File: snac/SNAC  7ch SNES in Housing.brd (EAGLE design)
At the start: 79.8 x 64.1 mm, 11 parts, among them U1 PMIC-LDO-XC6206P332MR-G(SOT23), X2 JST-XH-09-PIN-LONG-PAD

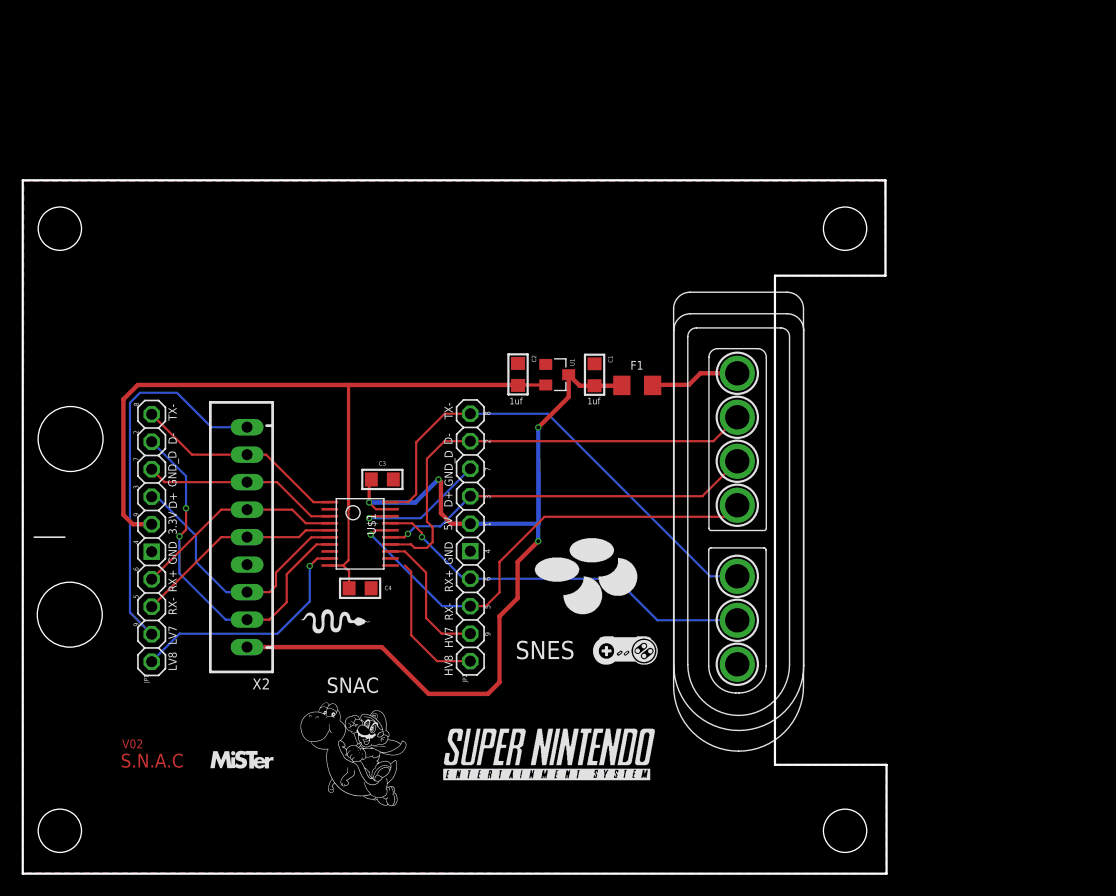
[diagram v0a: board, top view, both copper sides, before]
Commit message: Add Compact SNES version, and WIP SNES Multitap
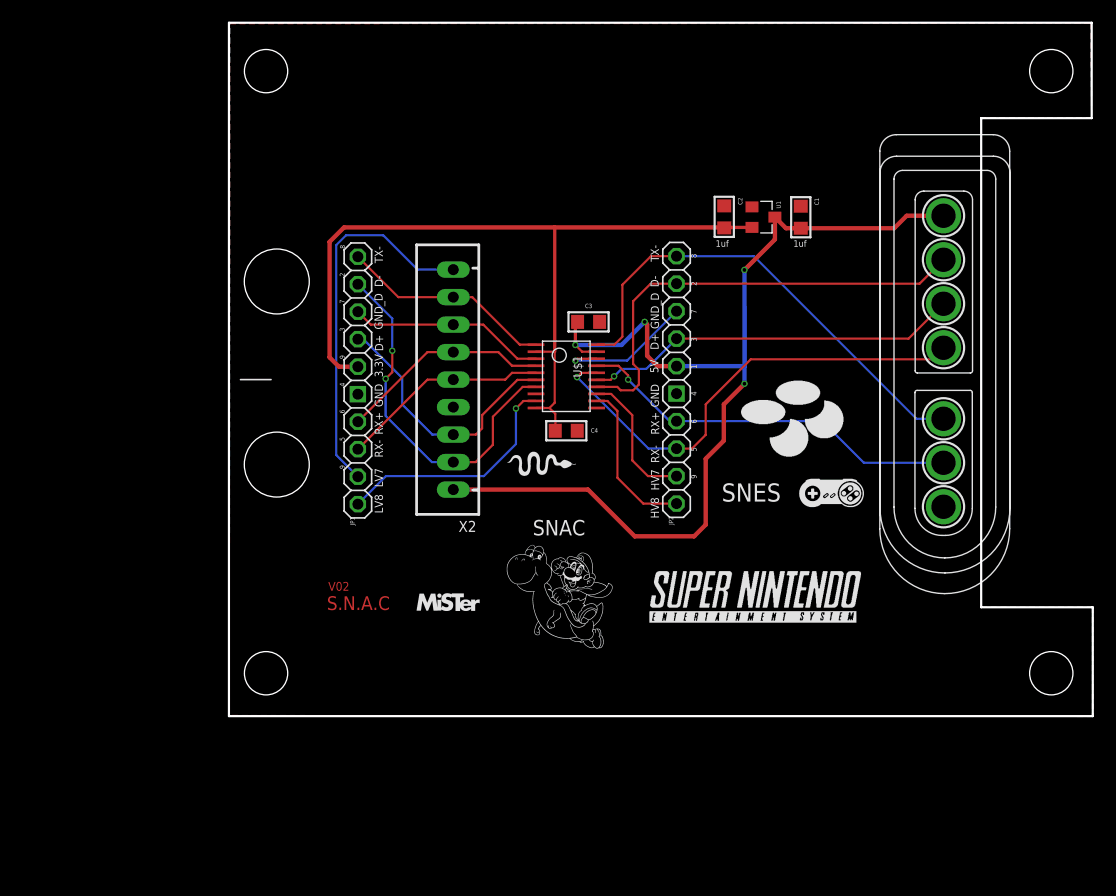
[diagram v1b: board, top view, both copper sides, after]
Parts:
- removed F1: 100mA, adafruit:R1206
- moved U$3 24.0 mm to (62.4, 46.8)
- moved JP1 24.0 mm to (12.4, 31.5)
- moved U$1 24.0 mm to (31.6, 31.9)
- moved U1 24.0 mm to (49.8, 46.6)
- moved C1 24.0 mm to (53.3, 46.6)
- moved C3 24.0 mm to (33.7, 37.0)
- moved C4 24.0 mm to (31.6, 26.9)
- moved JP2 24.0 mm to (41.8, 31.6)
- moved X2 24.0 mm to (21.2, 31.6)
- moved C2 24.0 mm to (46.2, 46.7)
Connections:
- removed net N$5: F1.2, U$3.5V
- net HV: now also U$3.5V; no longer F1.1
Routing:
- net HV: track 86.5 -> 97.7 mm
- net N$5: track 8.29 -> 0.00 mm
- net HV8: track 13.1 -> 14.9 mm
- net LV: track 73.7 -> 75.5 mm
